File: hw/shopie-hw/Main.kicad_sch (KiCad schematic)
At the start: 44 parts, among them J1 Jack-DC, J2 USB_B_Micro, J3 Conn_01x04_Socket, Q1 BSC016N06NS, SW1 SW_SPDT, SW2 SW_MEC_5E, SW3 SW_SPDT, U2 STM32F405RGT6, U3 LM2596T-5, U4 AP2112K-3.3, U6 MIC5365-1.8YC5, Y2 Crystal_Small

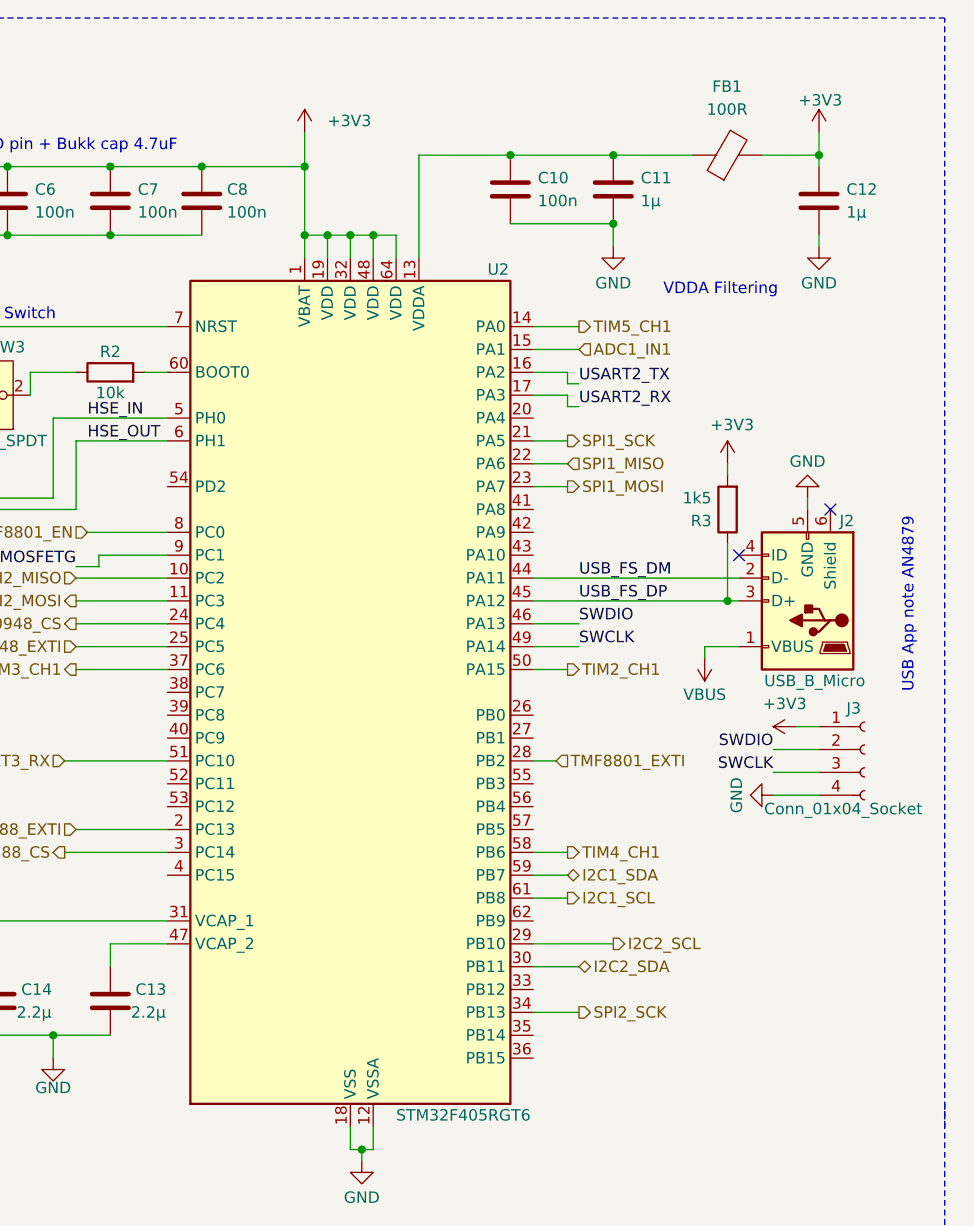
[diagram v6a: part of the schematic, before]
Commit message: Fix remaining schematic ERC issues
- Resolved all remaining ERC errors across schematic sheets
- All power input pins are driven by valid power sources
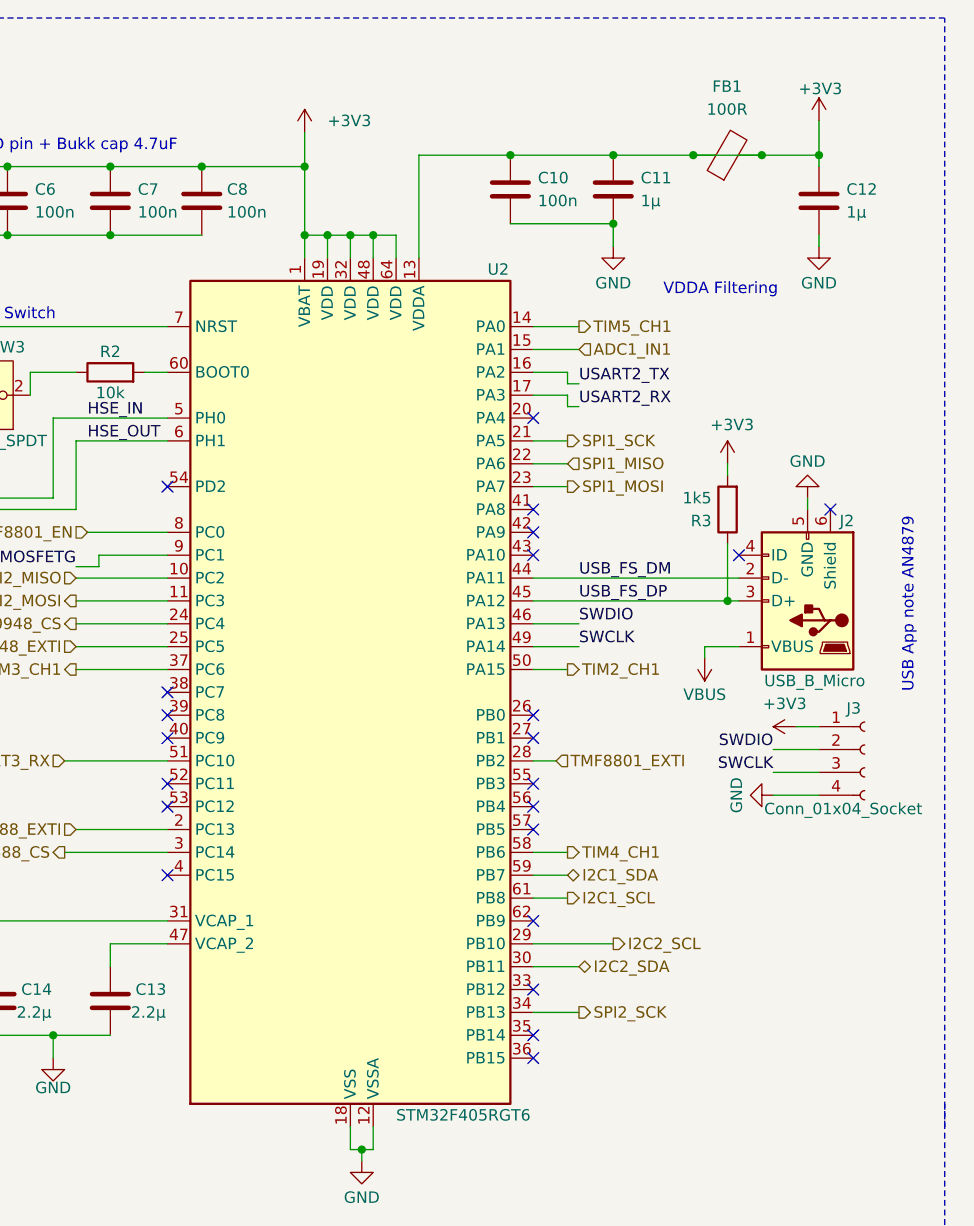
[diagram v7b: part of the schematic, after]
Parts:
- Q1: footprint BSC016N06NS:INF-PG-TDSON-8-FL -> ShopieLibrary:BSC016N06NS
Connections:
- net +3V3: now also C10.1, C11.1, FB1.1, U2.13 (VDDA)
- net VBAT_MAIN renamed 16V8
- no-connect marks 29 -> 49
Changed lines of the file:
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@@
 	)
 	(junction
+		(at 255.27 27.94)
+		(diameter 0)
+		(color 0 0 0 0)
+	)
+	(junction
 		(at 179.07 29.21)
 		(diameter 0)
@@
 	)
 	(junction
-		(at 269.24 27.94)
-		(diameter 0)
-		(color 0 0 0 0)
-	)
-	(junction
 		(at 46.99 127)
 		(diameter 0)
@@
 	)
 	(junction
+		(at 262.89 27.94)
+		(diameter 0)
+		(color 0 0 0 0)
+	)
+	(junction
 		(at 116.84 175.26)
 		(diameter 0)
@@
 	)
 	(junction
+		(at 269.24 27.94)
+		(diameter 0)
+		(color 0 0 0 0)
+	)
+	(junction
 		(at 234.95 27.94)
 		(diameter 0)
@@
 	)
 	(no_connect
+		(at 196.85 97.79)
+	)
+	(no_connect
 		(at 83.82 64.77)
 	)
@@
 	)
 	(no_connect
+		(at 237.49 120.65)
+	)
+	(no_connect
 		(at 83.82 49.53)
 	)
 	(no_connect
+		(at 237.49 90.17)
+	)
+	(no_connect
 		(at 48.26 64.77)
 	)
@@
 	)
 	(no_connect
+		(at 237.49 67.31)
+	)
+	(no_connect
+		(at 237.49 72.39)
+	)
+	(no_connect
+		(at 196.85 92.71)
+	)
+	(no_connect
 		(at 48.26 57.15)
 	)
@@
 	)
 	(no_connect
+		(at 237.49 102.87)
+	)
+	(no_connect
 		(at 156.21 49.53)
 	)
@@
 	)
 	(no_connect
+		(at 196.85 64.77)
+	)
+	(no_connect
+		(at 237.49 113.03)
+	)
+	(no_connect
+		(at 237.49 125.73)
+	)
+	(no_connect
+		(at 196.85 100.33)
+	)
+	(no_connect
+		(at 196.85 107.95)
+	)
+	(no_connect
 		(at 83.82 72.39)
 	)
 	(no_connect
+		(at 237.49 57.15)
+	)
+	(no_connect
 		(at 83.82 36.83)
 	)
@@
 	)
 	(no_connect
+		(at 237.49 92.71)
+	)
+	(no_connect
+		(at 237.49 100.33)
+	)
+	(no_connect
+		(at 196.85 90.17)
+	)
+	(no_connect
 		(at 83.82 62.23)
 	)
 	(no_connect
+		(at 237.49 69.85)
+	)
+	(no_connect
 		(at 48.26 44.45)
 	)
@@
 	)
 	(no_connect
+		(at 237.49 97.79)
+	)
+	(no_connect
+		(at 237.49 128.27)
+	)
+	(no_connect
+		(at 196.85 87.63)
+	)
+	(no_connect
 		(at 146.05 49.53)
 	)
@@
 	(wire
 		(pts
+			(xy 234.95 27.94) (xy 246.38 27.94)
+		)
+		(stroke
+			(width 0)
+			(type default)
+		)
+	)
+	(wire
+		(pts
 			(xy 160.02 57.15) (xy 160.02 58.42)
 		)
@@
 	(wire
 		(pts
-			(xy 269.24 25.4) (xy 269.24 27.94)
+			(xy 269.24 24.13) (xy 269.24 27.94)
 		)
 		(stroke
@@
 	(wire
 		(pts
+			(xy 255.27 27.94) (xy 246.38 27.94)
+		)
+		(stroke
+			(width 0)
+			(type default)
+		)
+	)
+	(wire
+		(pts
 			(xy 217.17 36.83) (xy 214.63 36.83)
 		)
@@
 	(wire
 		(pts
+			(xy 234.95 27.94) (xy 224.79 27.94)
+		)
+		(stroke
+			(width 0)
+			(type default)
+		)
+	)
+	(wire
+		(pts
 			(xy 68.58 184.15) (xy 69.85 184.15)
 		)
@@
 	(wire
 		(pts
-			(xy 246.38 27.94) (xy 255.27 27.94)
-		)
-		(stroke
-			(width 0)
-			(type default)
-		)
-	)
-	(wire
-		(pts
 			(xy 144.78 185.42) (xy 144.78 186.69)
 		)
@@
 	(wire
 		(pts
-			(xy 234.95 27.94) (xy 246.38 27.94)
-		)
-		(stroke
-			(width 0)
-			(type default)
-		)
-	)
-	(wire
-		(pts
 			(xy 157.48 146.05) (xy 161.29 146.05)
 		)
@@
 	(wire
 		(pts
-			(xy 269.24 27.94) (xy 262.89 27.94)
-		)
-		(stroke
-			(width 0)
-			(type default)
-		)
-	)
-	(wire
-		(pts
 			(xy 25.4 167.64) (xy 29.21 167.64)
 		)
@@
 	(wire
 		(pts
-			(xy 58.42 160.02) (xy 63.5 160.02)
+			(xy 269.24 27.94) (xy 262.89 27.94)
 		)
 		(stroke
@@
 	(wire
 		(pts
-			(xy 241.3 53.34) (xy 242.57 53.34)
+			(xy 58.42 160.02) (xy 63.5 160.02)
 		)
 		(stroke
@@
 	(wire
 		(pts
-			(xy 64.77 179.07) (xy 68.58 179.07)
+			(xy 241.3 53.34) (xy 242.57 53.34)
 		)
 		(stroke
@@
 	(wire
 		(pts
-			(xy 224.79 27.94) (xy 234.95 27.94)
+			(xy 64.77 179.07) (xy 68.58 179.07)
 		)
 		(stroke
@@
 	(wire
 		(pts
+			(xy 255.27 27.94) (xy 262.89 27.94)
+		)
+		(stroke
+			(width 0)
+			(type default)
+		)
+	)
+	(wire
+		(pts
 			(xy 256.54 83.82) (xy 256.54 82.55)
 		)
@@
 	)
 	(symbol
+		(lib_name "VCC_1")
 		(lib_id "power:VCC")
 		(at 92.71 115.57 270)
@@
 			)
 		)
-		(property "Description" "Power symbol creates a global label with name \"VCC\""
+		(property "Description" "A 16V8 Line coming straight from BMS output through a MOSFET."
 			(at 92.71 115.57 0)
 			(effects
@@
 	(symbol
 		(lib_id "power:+3.3V")
-		(at 269.24 25.4 0)
+		(at 269.24 24.13 0)
 		(unit 1)
 		(exclude_from_sim no)
@@
 		(dnp no)
 		(property "Reference" "#PWR026"
-			(at 269.24 29.21 0)
+			(at 269.24 27.94 0)
 			(effects
 				(font
@@
 		)
 		(property "Value" "+3V3"
-			(at 266.954 21.844 0)
+			(at 266.954 20.574 0)
 			(effects
 				(font
@@
 		)
 		(property "Footprint" ""
-			(at 269.24 25.4 0)
+			(at 269.24 24.13 0)
 			(effects
 				(font
@@
 		)
 		(property "Datasheet" ""
-			(at 269.24 25.4 0)
+			(at 269.24 24.13 0)
 			(effects
 				(font
@@
 		)
 		(property "Description" "Power symbol creates a global label with name \"+3.3V\""
-			(at 269.24 25.4 0)
+			(at 269.24 24.13 0)
 			(effects
 				(font
@@
 			)
 		)
-		(property "Footprint" "BSC016N06NS:INF-PG-TDSON-8-FL"
+		(property "Footprint" "ShopieLibrary:BSC016N06NS"
 			(at 53.34 124.46 0)
 			(effects

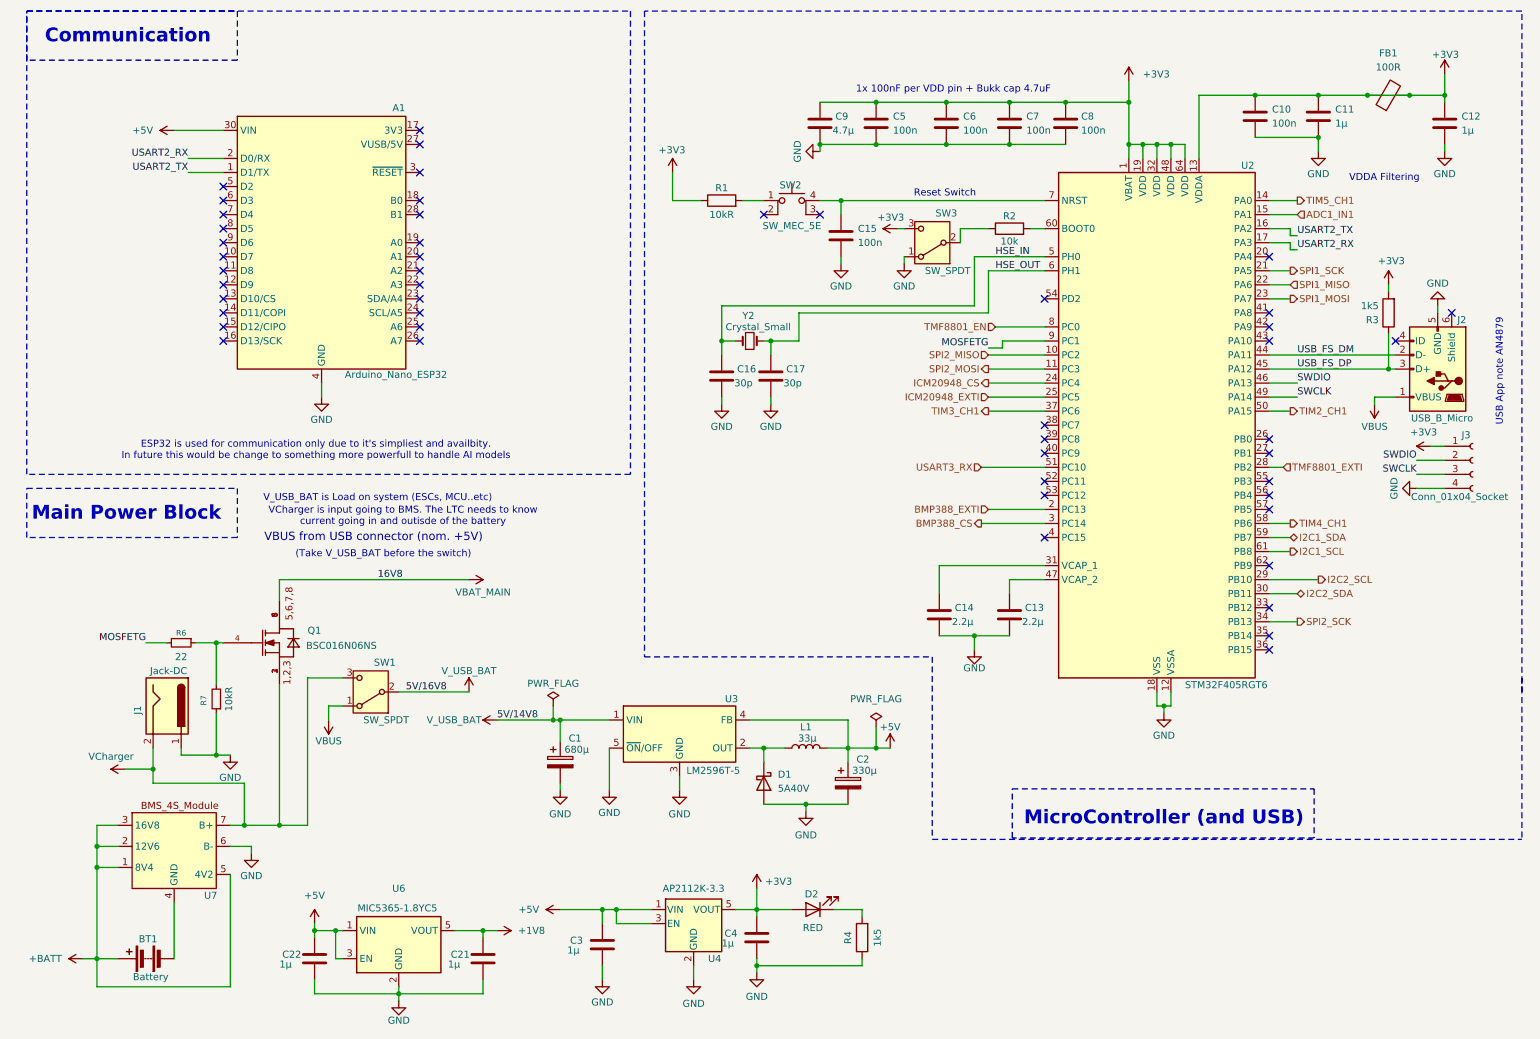
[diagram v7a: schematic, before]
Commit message: added/updated key components with symbols, footprints, and details
- Crystal Oscillator:
  • Replaced unavailable X49SM8MSD2SC (8MHz HC-49S-SMD) with X322512MSB4SI (12MHz, SMD3225-4P)
  • Added 22pF capacitors (CC0603JRNPO9BN220) to crystal OSC_IN and OSC_OUT, grounded both

- Power Switches:
  • Evaluated and replaced unavailable ST-0-102-C03-N003-RS with 2MS1T1B1M2QES toggle switch (SPDT, 2A@250VAC, 3A@28VDC)

- BOOT0 Slide Switch:
  • Added BOOT0 slide switch (50mA DPDT SMD vertical)
  • Connected 10kΩ pull-down resistor between switch output and GND
  • Enables manual BOOT0 control for programming mode

- ST-LINK Header:
  • Selected 1x5P 2.54mm THT header for SWD (SWCLK, SWDIO, GND, 3.3V, SWO)
  • SWO enabled via STM32CubeIDE “Trace Asynchronous SW” debug mode

-  JST-XH Battery Balance Connector:
  • Matched HRB 4S LiPo JST-XH (5 black + 1 red wire) to BMS cell input pins
  • To be paired with JST-XH 6-pin male connector on PCB

-  Barrel Jack:
  • Added Symbol for barrel Jack

All components(Caps, Resistors, etc..) added with valid footprints.
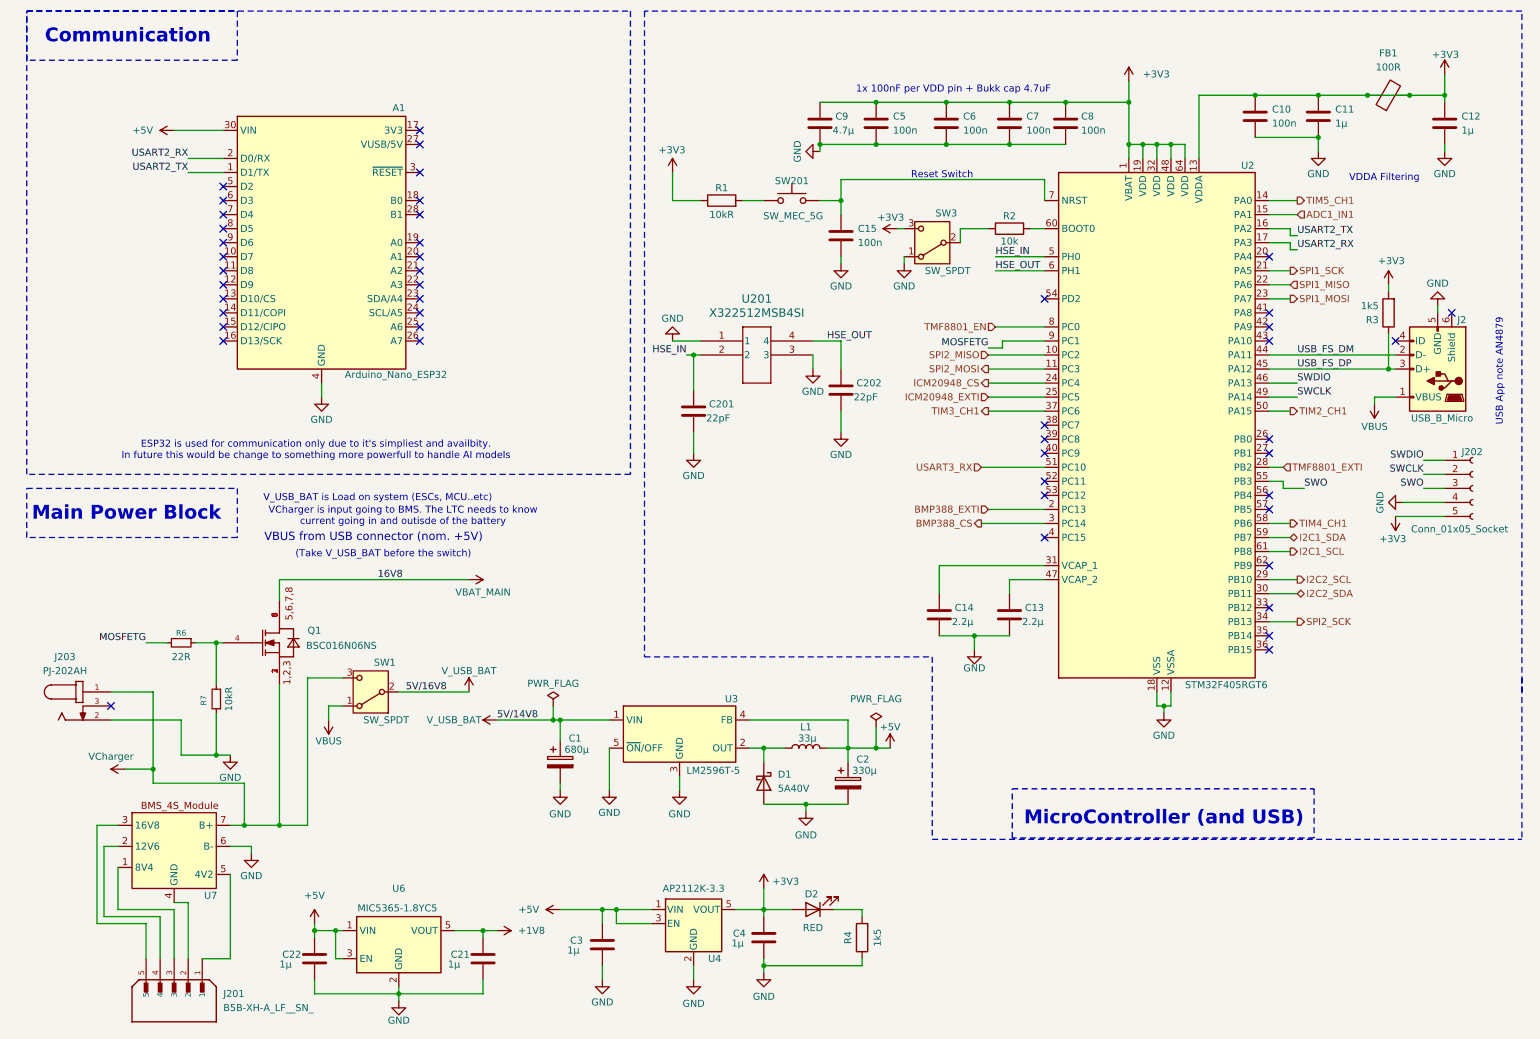
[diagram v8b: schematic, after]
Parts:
- removed BT1: Battery, symbol Device:Battery
- removed C16, C17: 30p, symbol Device:C
- removed J1: Jack-DC, symbol Connector:Jack-DC
- removed J3: Conn_01x04_Socket, symbol Connector:Conn_01x04_Socket
- removed SW2: SW_MEC_5E, symbol Switch:SW_MEC_5E
- removed Y2: Crystal_Small, symbol Device:Crystal_Small
- added C201, C202: 22pF, ShopieLibrary:CC0603JRNPO9BN220, symbol Device:C
- added J201: B5B-XH-A_LF__SN_, ShopieLibrary:JST_B5B-XH-A_LF__SN_, symbol shopie-hwLibrary:B5B-XH-A_LF__SN_
- added J202: Conn_01x05_Socket, ShopieLibrary:PZ254V-11-05P, symbol Connector:Conn_01x05_Socket
- added J203: PJ-202AH, ShopieLibrary:PJ-202AH, symbol shopie-hwLibrary:PJ-202AH
- added SW201: SW_MEC_5G, ShopieLibrary:TS-1088-AR02016, symbol Switch:SW_MEC_5G
- added U201: X322512MSB4SI, ShopieLibrary:2MSB4SI_YXC, symbol shopie-hwLibrary:X322512MSB4SI
- C1: footprint (none) -> Capacitor_THT:CP_Radial_D6.3mm_P2.50mm
- C10, C15, C5, C6, C7, C8: footprint (none) -> ShopieLibrary:CL21B104KBCNNNC
- C11, C12, C21, C22, C3, C4: footprint (none) -> ShopieLibrary:CL21B105KBFNNNE
- C13, C14: footprint (none) -> ShopieLibrary:CL21B225KAFNNNE
- C2: footprint (none) -> Capacitor_THT:CP_Radial_D10.0mm_P5.00mm
- C9: footprint (none) -> ShopieLibrary:CL31B475KBHNNNE
- D1: footprint (none) -> ShopieLibrary:1N5822
- D2: footprint (none) -> ShopieLibrary:15-21SURCS530-A33T
- FB1: footprint (none) -> ShopieLibrary:MPZ2012S101AT000
- L1: footprint (none) -> Inductor_SMD:L_Neosid_MicroCoil_Ms36-L
- R1, R2, R7: footprint (none) -> ShopieLibrary:RC0603FR-0710KL
- R3, R4: footprint (none) -> ShopieLibrary:WR06X1501FTL
- R6: value 22 -> 22R; footprint (none) -> ShopieLibrary:RC0603FR-0722RL
- SW1: footprint (none) -> ShopieLibrary:100SP3T1B1M2QE
- SW3: footprint (none) -> ShopieLibrary:MK-12C02-G020
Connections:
- net +3V3: now also J202.5 (Pin_5)
- net GND: now also C201.2, C202.2, J202.4 (Pin_4), J203.2, U201.1, U201.3
- net HSE_IN: now also C201.1, U201.2
- net HSE_OUT: now also C202.1, U201.4
- net SWCLK: now also J202.2 (Pin_2)
- net SWDIO: now also J202.1 (Pin_1)
- net VCharger: now also J203.1
- net at R1.2: now also SW201.1 (A), SW201.2 (A)
- net at C15.1, U2.7 (NRST): now also SW201.3 (B), SW201.4 (B)
- net at U7.4 (GND): now also J201.2
- net SWO: now reaches U2.55 (PB3)
- net SWO: now also J202.3 (Pin_3)
- removed net +BATT: U7.1 (8V4), U7.2 (12V6), U7.3 (16V8), U7.5 (4V2)
- new net: J201.3, U7.1 (8V4)
- new net: J201.4, U7.2 (12V6)
- new net: J201.5, U7.3 (16V8)
- new net: J201.1, U7.5 (4V2)
- no-connect marks 49 -> 47
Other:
- moved on the sheet: C4
